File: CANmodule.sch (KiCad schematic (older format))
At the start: 14 parts, among them J1 RJ45, U3 TLP2361, U4 TLP2361, U5 MCP2551-I/SN

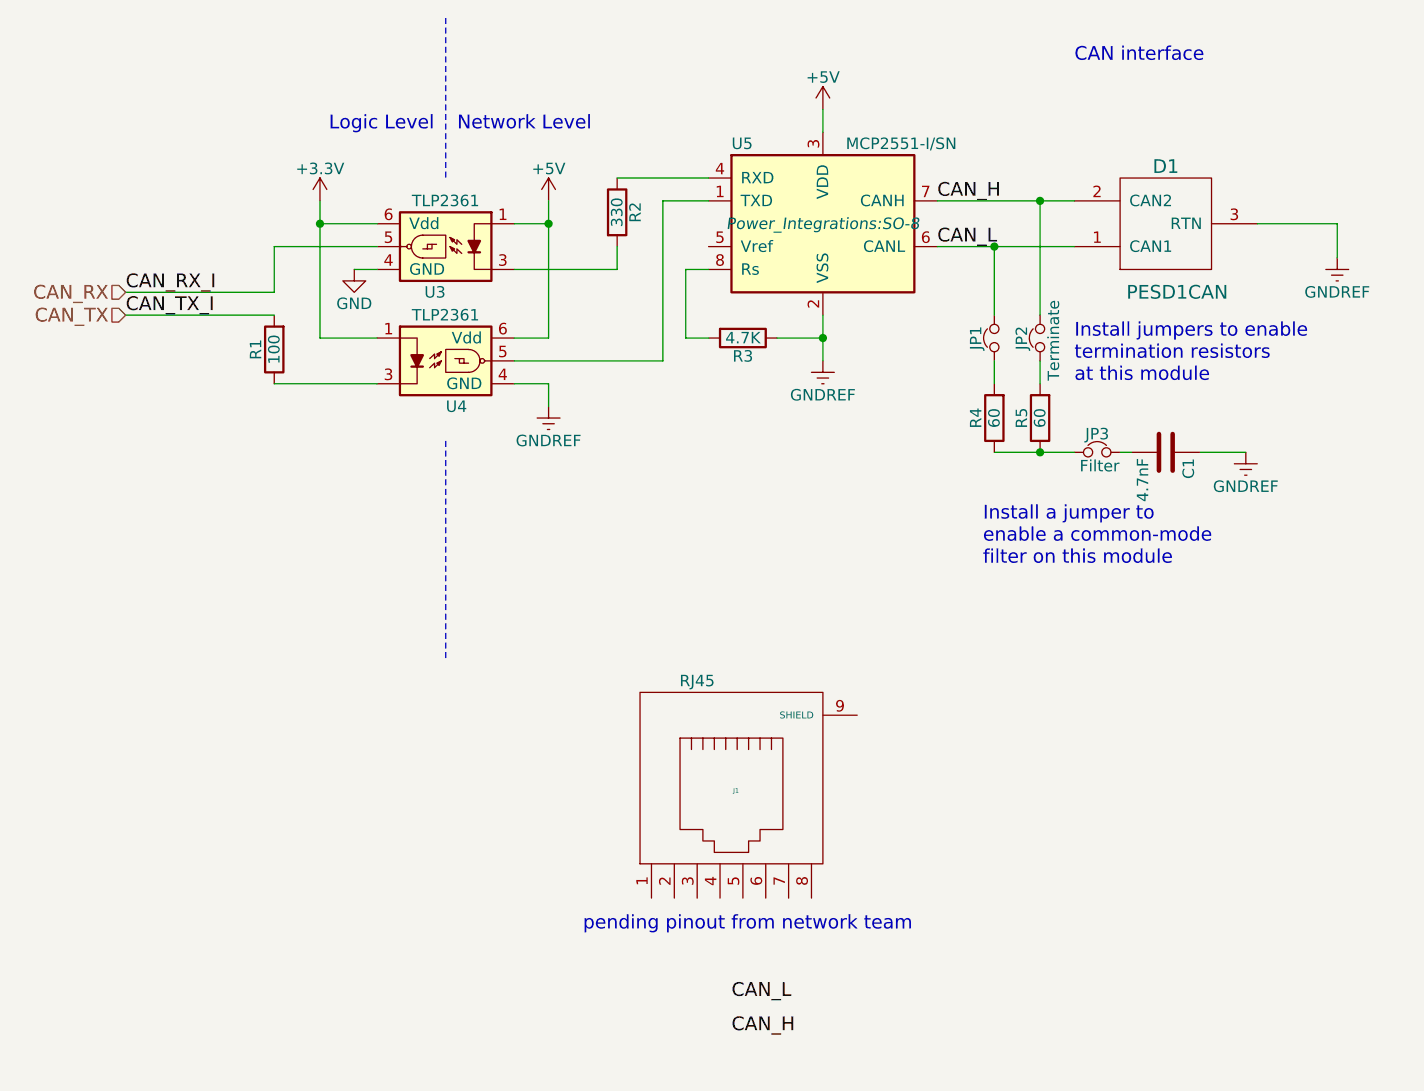
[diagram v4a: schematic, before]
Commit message: added hall-uC resistors for speed monitoring
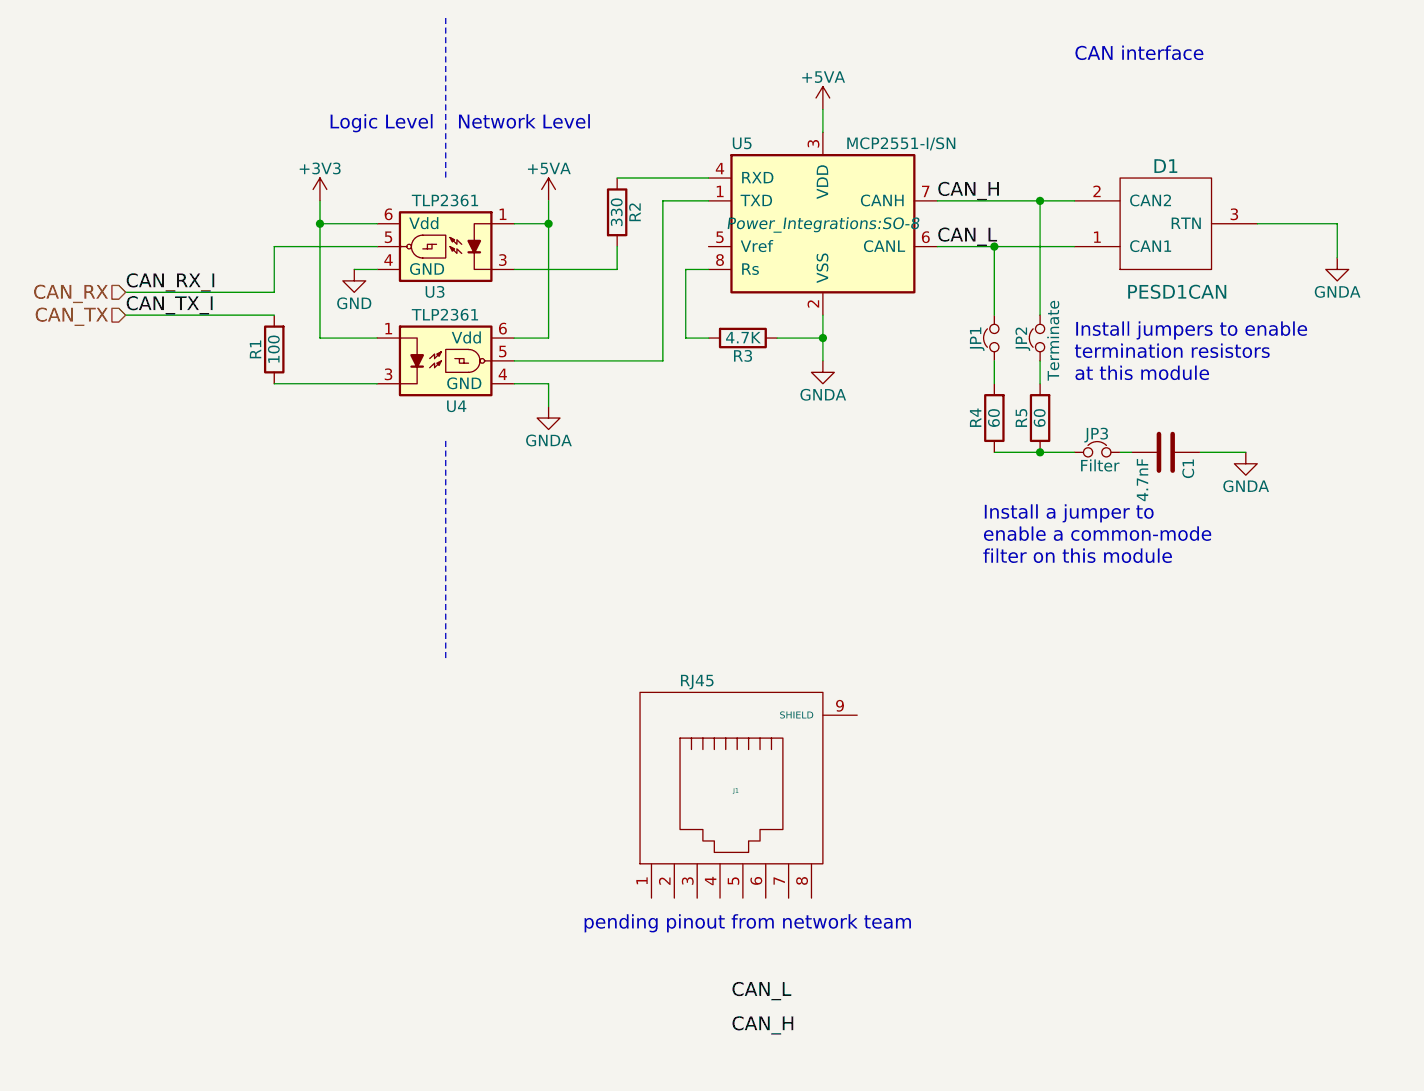
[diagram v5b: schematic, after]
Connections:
- net +5V renamed +5VA
- net GNDREF renamed GNDA
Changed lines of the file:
@@
 LIBS:contrib
 LIBS:valves
+LIBS:electric_car
 LIBS:Motor-interface-cache
 EELAYER 25 0
@@
 	-1   0    0    1
 $EndComp
-$Comp
-L GNDREF #PWR07
-U 1 1 57FCAEEC
-P 9050 2500
-F 0 "#PWR07" H 9050 2250 50  0001 C CNN
-F 1 "GNDREF" H 9050 2350 50  0000 C CNN
-F 2 "" H 9050 2500 50  0000 C CNN
-F 3 "" H 9050 2500 50  0000 C CNN
-	1    9050 2500
-	1    0    0    -1
-$EndComp
-$Comp
-L GNDREF #PWR08
-U 1 1 57FCAEED
-P 9450 1650
-F 0 "#PWR08" H 9450 1400 50  0001 C CNN
-F 1 "GNDREF" H 9450 1500 50  0000 C CNN
-F 2 "" H 9450 1650 50  0000 C CNN
-F 3 "" H 9450 1650 50  0000 C CNN
-	1    9450 1650
-	1    0    0    -1
-$EndComp
-$Comp
-L GNDREF #PWR09
-U 1 1 57FCAEEE
-P 7200 2100
-F 0 "#PWR09" H 7200 1850 50  0001 C CNN
-F 1 "GNDREF" H 7200 1950 50  0000 C CNN
-F 2 "" H 7200 2100 50  0000 C CNN
-F 3 "" H 7200 2100 50  0000 C CNN
-	1    7200 2100
-	1    0    0    -1
-$EndComp
-$Comp
-L +3.3V #PWR010
-U 1 1 57FCAEEF
-P 5000 1400
-F 0 "#PWR010" H 5000 1250 50  0001 C CNN
-F 1 "+3.3V" H 5000 1540 50  0000 C CNN
-F 2 "" H 5000 1400 50  0000 C CNN
-F 3 "" H 5000 1400 50  0000 C CNN
-	1    5000 1400
-	1    0    0    -1
-$EndComp
-$Comp
-L +5V #PWR011
-U 1 1 57FCAEF0
-P 6000 1400
-F 0 "#PWR011" H 6000 1250 50  0001 C CNN
-F 1 "+5V" H 6000 1540 50  0000 C CNN
-F 2 "" H 6000 1400 50  0000 C CNN
-F 3 "" H 6000 1400 50  0000 C CNN
-	1    6000 1400
-	1    0    0    -1
-$EndComp
-$Comp
-L +5V #PWR012
-U 1 1 57FCAEF1
-P 7200 1000
-F 0 "#PWR012" H 7200 850 50  0001 C CNN
-F 1 "+5V" H 7200 1140 50  0000 C CNN
-F 2 "" H 7200 1000 50  0000 C CNN
-F 3 "" H 7200 1000 50  0000 C CNN
-	1    7200 1000
-	1    0    0    -1
-$EndComp
 Text Label 7700 1400 0    60   ~ 0
 CAN_H
@@
 	1    0    0    -1
 $EndComp
-$Comp
-L GNDREF #PWR014
-U 1 1 57FCAEFC
-P 6000 2300
-F 0 "#PWR014" H 6000 2050 50  0001 C CNN
-F 1 "GNDREF" H 6000 2150 50  0000 C CNN
-F 2 "" H 6000 2300 50  0000 C CNN
-F 3 "" H 6000 2300 50  0000 C CNN
-	1    6000 2300
-	1    0    0    -1
-$EndComp
 Text Label 4150 1800 0    60   ~ 0
 CAN_RX_I
@@
 Text Notes 6150 4600 0    60   ~ 0
 pending pinout from network team
+$Comp
+L +5VA #PWR?
+U 1 1 582A8343
+P 6000 1400
+F 0 "#PWR?" H 6000 1250 50  0001 C CNN
+F 1 "+5VA" H 6000 1540 50  0000 C CNN
+F 2 "" H 6000 1400 50  0000 C CNN
+F 3 "" H 6000 1400 50  0000 C CNN
+	1    6000 1400
+	1    0    0    -1
+$EndComp
+$Comp
+L +5VA #PWR?
+U 1 1 582A84BF
+P 7200 1000
+F 0 "#PWR?" H 7200 850 50  0001 C CNN
+F 1 "+5VA" H 7200 1140 50  0000 C CNN
+F 2 "" H 7200 1000 50  0000 C CNN
+F 3 "" H 7200 1000 50  0000 C CNN
+	1    7200 1000
+	1    0    0    -1
+$EndComp
+$Comp
+L GNDA #PWR?
+U 1 1 582A8520
+P 6000 2300
+F 0 "#PWR?" H 6000 2050 50  0001 C CNN
+F 1 "GNDA" H 6000 2150 50  0000 C CNN
+F 2 "" H 6000 2300 50  0000 C CNN
+F 3 "" H 6000 2300 50  0000 C CNN
+	1    6000 2300
+	1    0    0    -1
+$EndComp
+$Comp
+L GNDA #PWR?
+U 1 1 582A8593
+P 7200 2100
+F 0 "#PWR?" H 7200 1850 50  0001 C CNN
+F 1 "GNDA" H 7200 1950 50  0000 C CNN
+F 2 "" H 7200 2100 50  0000 C CNN
+F 3 "" H 7200 2100 50  0000 C CNN
+	1    7200 2100
+	1    0    0    -1
+$EndComp
+$Comp
+L GNDA #PWR?
+U 1 1 582A864A
+P 9450 1650
+F 0 "#PWR?" H 9450 1400 50  0001 C CNN
+F 1 "GNDA" H 9450 1500 50  0000 C CNN
+F 2 "" H 9450 1650 50  0000 C CNN
+F 3 "" H 9450 1650 50  0000 C CNN
+	1    9450 1650
+	1    0    0    -1
+$EndComp
+$Comp
+L GNDA #PWR?
+U 1 1 582A86D1
+P 9050 2500
+F 0 "#PWR?" H 9050 2250 50  0001 C CNN
+F 1 "GNDA" H 9050 2350 50  0000 C CNN
+F 2 "" H 9050 2500 50  0000 C CNN
+F 3 "" H 9050 2500 50  0000 C CNN
+	1    9050 2500
+	1    0    0    -1
+$EndComp
+$Comp
+L +3V3 #PWR?
+U 1 1 582A8930
+P 5000 1400
+F 0 "#PWR?" H 5000 1250 50  0001 C CNN
+F 1 "+3V3" H 5000 1540 50  0000 C CNN
+F 2 "" H 5000 1400 50  0000 C CNN
+F 3 "" H 5000 1400 50  0000 C CNN
+	1    5000 1400
+	1    0    0    -1
+$EndComp
 $EndSCHEMATC

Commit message: Isolated the Motor Controller, added PSU
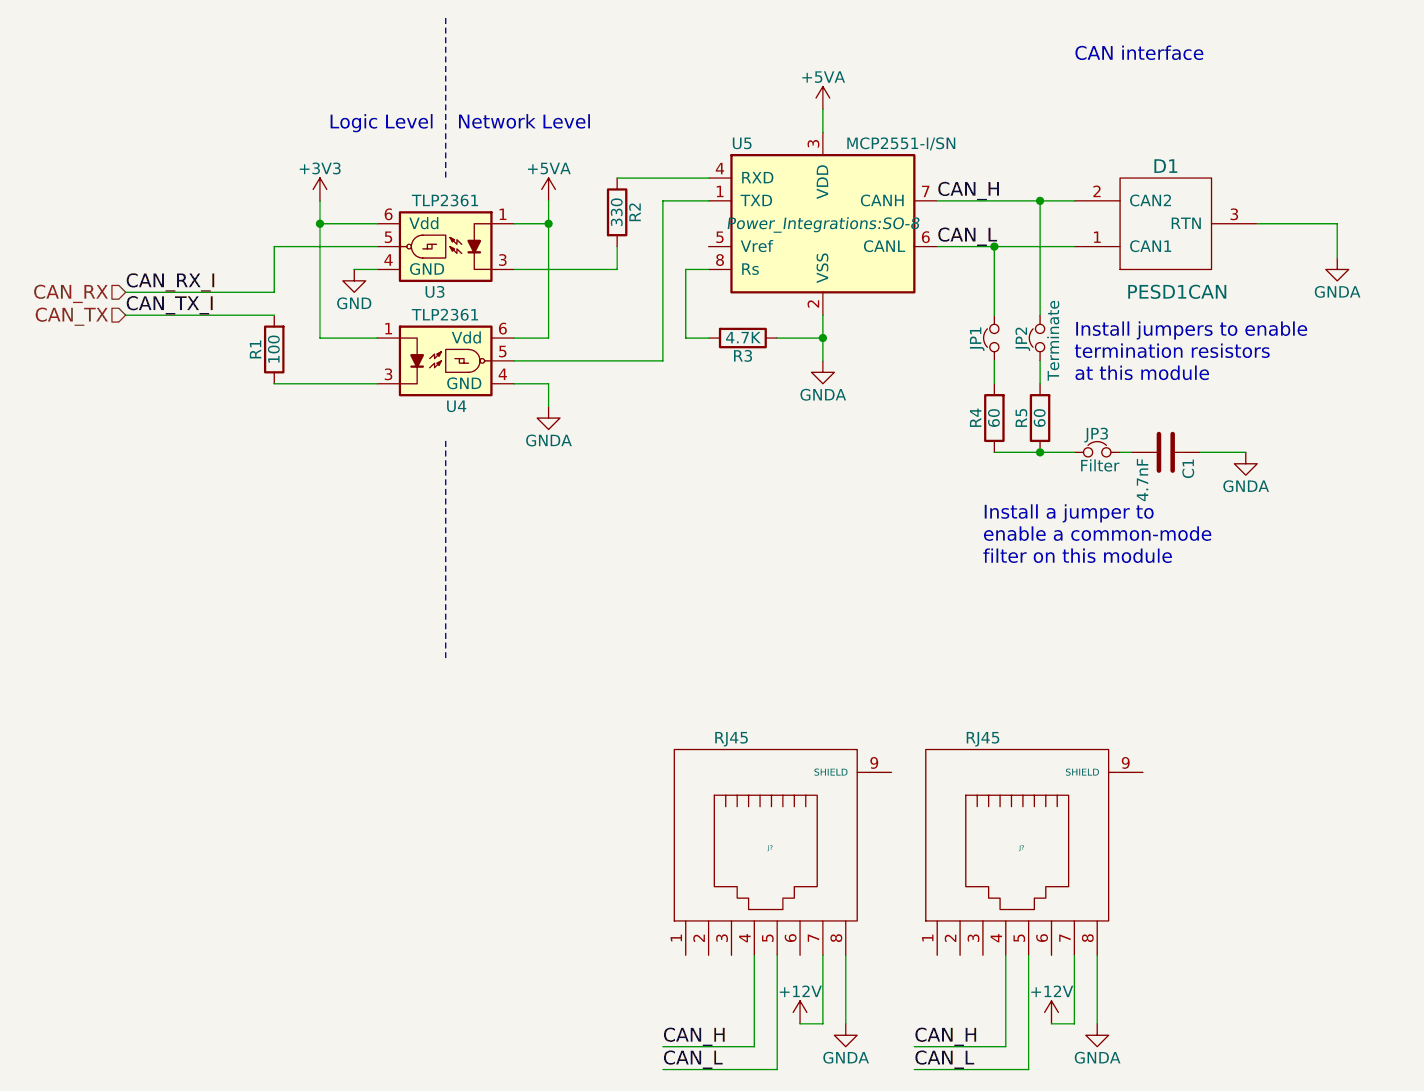
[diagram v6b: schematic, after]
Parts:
- removed J1: RJ45, Connect:RJ45_8, symbol RJ45
- added J? (x2): RJ45, Connect:RJ45_8, symbol RJ45
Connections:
- net CAN_H: now also J?.4, J?.4
- net CAN_L: now also J?.5, J?.5
- net GNDA: now also J?.8, J?.8
- new net +12V: J?.7, J?.7
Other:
- note removed: "pending pinout from network team"
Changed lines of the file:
@@
 $Descr A4 11693 8268
 encoding utf-8
-Sheet 2 2
+Sheet 2 3
 Title "CAN adapter"
 Date "2016-02-02"
@@
 	7000 2000 7200 2000
 Wire Wire Line
-	7200 1900 7200 2100
+	7200 1900 7200 2000
+Wire Wire Line
+	7200 2000 7200 2100
 Connection ~ 7200 2000
 Wire Wire Line
-	7700 1600 8300 1600
-Wire Wire Line
-	7700 1400 8300 1400
+	7700 1600 7950 1600
+Wire Wire Line
+	7950 1600 8300 1600
+Wire Wire Line
+	7700 1400 8150 1400
+Wire Wire Line
+	8150 1400 8300 1400
 Connection ~ 7950 1600
 Connection ~ 8150 1400
@@
 	4800 1600 5250 1600
 Wire Wire Line
-	5000 1400 5000 2000
+	5000 1400 5000 1500
+Wire Wire Line
+	5000 1500 5000 2000
 Wire Wire Line
 	5850 1500 6000 1500
 Wire Wire Line
-	6000 1400 6000 2000
+	6000 1400 6000 1500
+Wire Wire Line
+	6000 1500 6000 2000
 Wire Wire Line
 	7200 1000 7200 1100
@@
 	8150 2100 8150 2200
 Wire Wire Line
-	7950 2500 8300 2500
+	7950 2500 8150 2500
+Wire Wire Line
+	8150 2500 8300 2500
 Wire Wire Line
 	4150 1800 4800 1800
@@
 Text HLabel 4150 1800 0    60   Input ~ 0
 CAN_RX
-$Comp
-L RJ45 J1
-U 1 1 57FCC775
-P 6800 4000
-F 0 "J1" H 6820 4020 20  0000 C CNN
-F 1 "RJ45" H 6650 4500 50  0000 C CNN
-F 2 "Connect:RJ45_8" H 6800 4000 50  0001 C CNN
-F 3 "" H 6800 4000 50  0000 C CNN
-	1    6800 4000
-	1    0    0    -1
-$EndComp
 Wire Notes Line
 	5550 2450 5550 3400
-Text Label 6800 5050 0    60   ~ 0
+Text Label 7600 5100 0    60   ~ 0
 CAN_H
-Text Label 6800 4900 0    60   ~ 0
+Text Label 7600 5200 0    60   ~ 0
 CAN_L
-Text Notes 6150 4600 0    60   ~ 0
-pending pinout from network team
 $Comp
 L +5VA #PWR?
@@
 	1    0    0    -1
 $EndComp
+$Comp
+L RJ45 J?
+U 1 1 582DA582
+P 8050 4250
+F 0 "J?" H 8070 4270 20  0000 C CNN
+F 1 "RJ45" H 7900 4750 50  0000 C CNN
+F 2 "Connect:RJ45_8" H 8050 4250 50  0001 C CNN
+F 3 "" H 8050 4250 50  0000 C CNN
+	1    8050 4250
+	1    0    0    -1
+$EndComp
+$Comp
+L +12V #PWR?
+U 1 1 582DA73C
+P 8200 5000
+F 0 "#PWR?" H 8200 4850 50  0001 C CNN
+F 1 "+12V" H 8200 5140 50  0000 C CNN
+F 2 "" H 8200 5000 50  0000 C CNN
+F 3 "" H 8200 5000 50  0000 C CNN
+	1    8200 5000
+	1    0    0    -1
+$EndComp
+$Comp
+L GNDA #PWR?
+U 1 1 582DA7E4
+P 8400 5000
+F 0 "#PWR?" H 8400 4750 50  0001 C CNN
+F 1 "GNDA" H 8400 4850 50  0000 C CNN
+F 2 "" H 8400 5000 50  0000 C CNN
+F 3 "" H 8400 5000 50  0000 C CNN
+	1    8400 5000
+	1    0    0    -1
+$EndComp
+Wire Wire Line
+	8400 5000 8400 4700
+Wire Wire Line
+	7600 5200 8100 5200
+Wire Wire Line
+	8100 5200 8100 4700
+Wire Wire Line
+	7600 5100 8000 5100
+Wire Wire Line
+	8000 5100 8000 4700
+Wire Wire Line
+	8200 5000 8300 5000
+Wire Wire Line
+	8300 5000 8300 4700
+Text Label 6500 5100 0    60   ~ 0
+CAN_H
+Text Label 6500 5200 0    60   ~ 0
+CAN_L
+$Comp
+L RJ45 J?
+U 1 1 582DC5CA
+P 6950 4250
+F 0 "J?" H 6970 4270 20  0000 C CNN
+F 1 "RJ45" H 6800 4750 50  0000 C CNN
+F 2 "Connect:RJ45_8" H 6950 4250 50  0001 C CNN
+F 3 "" H 6950 4250 50  0000 C CNN
+	1    6950 4250
+	1    0    0    -1
+$EndComp
+$Comp
+L +12V #PWR?
+U 1 1 582DC5D0
+P 7100 5000
+F 0 "#PWR?" H 7100 4850 50  0001 C CNN
+F 1 "+12V" H 7100 5140 50  0000 C CNN
+F 2 "" H 7100 5000 50  0000 C CNN
+F 3 "" H 7100 5000 50  0000 C CNN
+	1    7100 5000
+	1    0    0    -1
+$EndComp
+$Comp
+L GNDA #PWR?
+U 1 1 582DC5D6
+P 7300 5000
+F 0 "#PWR?" H 7300 4750 50  0001 C CNN
+F 1 "GNDA" H 7300 4850 50  0000 C CNN
+F 2 "" H 7300 5000 50  0000 C CNN
+F 3 "" H 7300 5000 50  0000 C CNN
+	1    7300 5000
+	1    0    0    -1
+$EndComp
+Wire Wire Line
+	7300 5000 7300 4700
+Wire Wire Line
+	6500 5200 7000 5200
+Wire Wire Line
+	7000 5200 7000 4700
+Wire Wire Line
+	6500 5100 6900 5100
+Wire Wire Line
+	6900 5100 6900 4700
+Wire Wire Line
+	7100 5000 7200 5000
+Wire Wire Line
+	7200 5000 7200 4700
 $EndSCHEMATC
